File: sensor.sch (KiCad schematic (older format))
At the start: 6 parts

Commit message: switched to sensor sheet for one sensor divider
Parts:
- gave numbers to parts that had none: 6

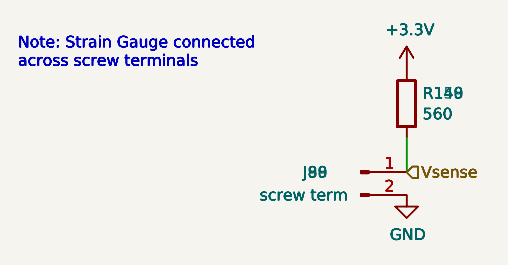
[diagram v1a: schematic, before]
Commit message: updated screw terminals to 2.54mm
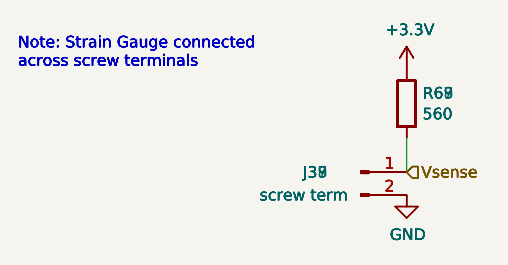
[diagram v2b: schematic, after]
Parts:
- J3: footprint Connector_PinHeader_1.27mm:PinHeader_1x02_P1.27mm_Vertical -> Connector_PinHeader_2.54mm:PinHeader_1x02_P2.54mm_Vertical
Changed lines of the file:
@@
 $Descr A4 11693 8268
 encoding utf-8
-Sheet 3 41
+Sheet 19 41
 Title ""
 Date ""
@@
 AR Path="/601B4C19/601A6FD1/6019C1B1" Ref="#PWR0181"  Part="1"
 AR Path="/601B4C19/601A6FD6/6019C1B1" Ref="#PWR0187"  Part="1"
-F 0 "#PWR0233" H 5400 3350 50  0001 C CNN
+F 0 "#PWR0110" H 5400 3350 50  0001 C CNN
 F 1 "GND" H 5405 3427 50  0000 C CNN
 F 2 "" H 5400 3600 50  0001 C CNN
@@
 AR Path="/601B4C19/601A6FD1/6019C1B2" Ref="R117"  Part="1"
 AR Path="/601B4C19/601A6FD6/6019C1B2" Ref="R120"  Part="1"
-F 0 "R150" H 5470 3246 50  0000 L CNN
+F 0 "R69" H 5470 3246 50  0000 L CNN
 F 1 "560" H 5470 3155 50  0000 L CNN
 F 2 "Resistor_THT:R_Axial_DIN0204_L3.6mm_D1.6mm_P5.08mm_Horizontal" V 5330 3200 50  0001 C CNN
@@
 AR Path="/601B4C19/601A6FD1/6019C1B3" Ref="J69"  Part="1"
 AR Path="/601B4C19/601A6FD6/6019C1B3" Ref="J72"  Part="1"
-F 0 "J90" H 5000 3500 50  0000 C CNN
+F 0 "J39" H 5000 3500 50  0000 C CNN
 F 1 "screw term" H 4950 3400 50  0000 C CNN
-F 2 "Connector_PinHeader_1.27mm:PinHeader_1x02_P1.27mm_Vertical" H 5200 3500 50  0001 C CNN
+F 2 "Connector_PinHeader_2.54mm:PinHeader_1x02_P2.54mm_Vertical" H 5200 3500 50  0001 C CNN
 F 3 "~" H 5200 3500 50  0001 C CNN
 	1    5200 3500
@@
 AR Path="/601B4C19/601A6FD1/601968DA" Ref="#PWR0176"  Part="1"
 AR Path="/601B4C19/601A6FD6/601968DA" Ref="#PWR0182"  Part="1"
-F 0 "#PWR0228" H 5400 2900 50  0001 C CNN
+F 0 "#PWR0105" H 5400 2900 50  0001 C CNN
 F 1 "+3.3V" H 5415 3223 50  0000 C CNN
 F 2 "" H 5400 3050 50  0001 C CNN
@@
 AR Path="/601B4C19/601A6FD1/6019BD32" Ref="#PWR0180"  Part="1"
 AR Path="/601B4C19/601A6FD6/6019BD32" Ref="#PWR0186"  Part="1"
-F 0 "#PWR0232" H 5400 3350 50  0001 C CNN
+F 0 "#PWR0109" H 5400 3350 50  0001 C CNN
 F 1 "GND" H 5405 3427 50  0000 C CNN
 F 2 "" H 5400 3600 50  0001 C CNN
@@
 AR Path="/601B4C19/601A6FD1/6019BD33" Ref="R116"  Part="1"
 AR Path="/601B4C19/601A6FD6/6019BD33" Ref="R119"  Part="1"
-F 0 "R149" H 5470 3246 50  0000 L CNN
+F 0 "R68" H 5470 3246 50  0000 L CNN
 F 1 "560" H 5470 3155 50  0000 L CNN
 F 2 "Resistor_THT:R_Axial_DIN0204_L3.6mm_D1.6mm_P5.08mm_Horizontal" V 5330 3200 50  0001 C CNN
@@
 AR Path="/601B4C19/601A6FD1/6019BD34" Ref="J68"  Part="1"
 AR Path="/601B4C19/601A6FD6/6019BD34" Ref="J71"  Part="1"
-F 0 "J89" H 5000 3500 50  0000 C CNN
+F 0 "J38" H 5000 3500 50  0000 C CNN
 F 1 "screw term" H 4950 3400 50  0000 C CNN
 F 2 "Connector_PinHeader_1.27mm:PinHeader_1x02_P1.27mm_Vertical" H 5200 3500 50  0001 C CNN
@@
 	1    0    0    -1
 $EndComp
-Wire Wire Line
-	5400 3350 5400 3500
 $Comp
 L power:+3.3V #PWR016
@@
 AR Path="/601B4C19/601A6FD1/6019BD35" Ref="#PWR0177"  Part="1"
 AR Path="/601B4C19/601A6FD6/6019BD35" Ref="#PWR0183"  Part="1"
-F 0 "#PWR0229" H 5400 2900 50  0001 C CNN
+F 0 "#PWR0106" H 5400 2900 50  0001 C CNN
 F 1 "+3.3V" H 5415 3223 50  0000 C CNN
 F 2 "" H 5400 3050 50  0001 C CNN
@@
 AR Path="/601B4C19/601A6FD1/60194B46" Ref="#PWR0179"  Part="1"
 AR Path="/601B4C19/601A6FD6/60194B46" Ref="#PWR0185"  Part="1"
-F 0 "#PWR0231" H 5400 3350 50  0001 C CNN
+F 0 "#PWR0108" H 5400 3350 50  0001 C CNN
 F 1 "GND" H 5405 3427 50  0000 C CNN
 F 2 "" H 5400 3600 50  0001 C CNN
@@
 AR Path="/601B4C19/601A6FD1/60194B4C" Ref="R115"  Part="1"
 AR Path="/601B4C19/601A6FD6/60194B4C" Ref="R118"  Part="1"
-F 0 "R148" H 5470 3246 50  0000 L CNN
+F 0 "R67" H 5470 3246 50  0000 L CNN
 F 1 "560" H 5470 3155 50  0000 L CNN
 F 2 "Resistor_THT:R_Axial_DIN0204_L3.6mm_D1.6mm_P5.08mm_Horizontal" V 5330 3200 50  0001 C CNN
@@
 AR Path="/601B4C19/601A6FD1/60194E45" Ref="J67"  Part="1"
 AR Path="/601B4C19/601A6FD6/60194E45" Ref="J70"  Part="1"
-F 0 "J88" H 5000 3500 50  0000 C CNN
+F 0 "J37" H 5000 3500 50  0000 C CNN
 F 1 "screw term" H 4950 3400 50  0000 C CNN
 F 2 "Connector_PinHeader_1.27mm:PinHeader_1x02_P1.27mm_Vertical" H 5200 3500 50  0001 C CNN
@@
 	1    0    0    -1
 $EndComp
-Wire Wire Line
-	5400 3350 5400 3500
 $Comp
 L power:+3.3V #PWR017
@@
 AR Path="/601B4C19/601A6FD1/6019C1B4" Ref="#PWR0178"  Part="1"
 AR Path="/601B4C19/601A6FD6/6019C1B4" Ref="#PWR0184"  Part="1"
-F 0 "#PWR0230" H 5400 2900 50  0001 C CNN
+F 0 "#PWR0107" H 5400 2900 50  0001 C CNN
 F 1 "+3.3V" H 5415 3223 50  0000 C CNN
 F 2 "" H 5400 3050 50  0001 C CNN

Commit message: removed stacked components
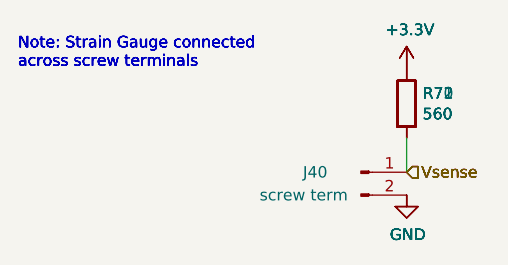
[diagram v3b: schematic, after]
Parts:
- removed J2: screw term, Connector_PinHeader_1.27mm:PinHeader_1x02_P1.27mm_Vertical, symbol Connector:Conn_01x02_Male
- removed J3: screw term, Connector_PinHeader_2.54mm:PinHeader_1x02_P2.54mm_Vertical, symbol Connector:Conn_01x02_Male
- J1: footprint Connector_PinHeader_1.27mm:PinHeader_1x02_P1.27mm_Vertical -> Connector_PinHeader_2.54mm:PinHeader_1x02_P2.54mm_Vertical
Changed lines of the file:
@@
 $Descr A4 11693 8268
 encoding utf-8
-Sheet 19 41
+Sheet 3 41
 Title ""
 Date ""
@@
 AR Path="/601B4C19/601A6FD1/6019C1B1" Ref="#PWR0181"  Part="1"
 AR Path="/601B4C19/601A6FD6/6019C1B1" Ref="#PWR0187"  Part="1"
-F 0 "#PWR0110" H 5400 3350 50  0001 C CNN
+F 0 "#PWR0116" H 5400 3350 50  0001 C CNN
 F 1 "GND" H 5405 3427 50  0000 C CNN
 F 2 "" H 5400 3600 50  0001 C CNN
@@
 AR Path="/601B4C19/601A6FD1/6019C1B2" Ref="R117"  Part="1"
 AR Path="/601B4C19/601A6FD6/6019C1B2" Ref="R120"  Part="1"
-F 0 "R69" H 5470 3246 50  0000 L CNN
+F 0 "R72" H 5470 3246 50  0000 L CNN
 F 1 "560" H 5470 3155 50  0000 L CNN
 F 2 "Resistor_THT:R_Axial_DIN0204_L3.6mm_D1.6mm_P5.08mm_Horizontal" V 5330 3200 50  0001 C CNN
 F 3 "~" H 5400 3200 50  0001 C CNN
 	1    5400 3200
-	1    0    0    -1
-$EndComp
-$Comp
-L Connector:Conn_01x02_Male J3
-U 1 1 6019C1B3
-P 5200 3500
-AR Path="/6017CC5E/60194350/6019C1B3" Ref="J3"  Part="1"
-AR Path="/6017CC5E/6019B999/6019C1B3" Ref="J6"  Part="1"
-AR Path="/601B4C0E/60194350/6019C1B3" Ref="J39"  Part="1"
-AR Path="/601B4C0E/6019B999/6019C1B3" Ref="J42"  Part="1"
-AR Path="/601B73B7/60194350/6019C1B3" Ref="J75"  Part="1"
-AR Path="/601B73B7/6019B999/6019C1B3" Ref="J78"  Part="1"
-AR Path="/6017CC5E/6019BDB6/6019C1B3" Ref="J9"  Part="1"
-AR Path="/601B4C0E/6019BDB6/6019C1B3" Ref="J45"  Part="1"
-AR Path="/601B73B7/6019BDB6/6019C1B3" Ref="J81"  Part="1"
-AR Path="/601927EB/601A1EA6/6019C1B3" Ref="J12"  Part="1"
-AR Path="/601927EB/601A1EAB/6019C1B3" Ref="J15"  Part="1"
-AR Path="/601927EB/601A1EB0/6019C1B3" Ref="J18"  Part="1"
-AR Path="/601B4C11/601A1EA6/6019C1B3" Ref="J48"  Part="1"
-AR Path="/601B4C11/601A1EAB/6019C1B3" Ref="J51"  Part="1"
-AR Path="/601B4C11/601A1EB0/6019C1B3" Ref="J54"  Part="1"
-AR Path="/601B73BA/601A1EA6/6019C1B3" Ref="J84"  Part="1"
-AR Path="/601B73BA/601A1EAB/6019C1B3" Ref="J87"  Part="1"
-AR Path="/601B73BA/601A1EB0/6019C1B3" Ref="J90"  Part="1"
-AR Path="/6019C043/601A47AA/6019C1B3" Ref="J21"  Part="1"
-AR Path="/6019C043/601A47AF/6019C1B3" Ref="J24"  Part="1"
-AR Path="/6019C043/601A47B4/6019C1B3" Ref="J27"  Part="1"
-AR Path="/601B4C16/601A47AA/6019C1B3" Ref="J57"  Part="1"
-AR Path="/601B4C16/601A47AF/6019C1B3" Ref="J60"  Part="1"
-AR Path="/601B4C16/601A47B4/6019C1B3" Ref="J63"  Part="1"
-AR Path="/6019DBCE/601A6FCC/6019C1B3" Ref="J30"  Part="1"
-AR Path="/6019DBCE/601A6FD1/6019C1B3" Ref="J33"  Part="1"
-AR Path="/6019DBCE/601A6FD6/6019C1B3" Ref="J36"  Part="1"
-AR Path="/601B4C19/601A6FCC/6019C1B3" Ref="J66"  Part="1"
-AR Path="/601B4C19/601A6FD1/6019C1B3" Ref="J69"  Part="1"
-AR Path="/601B4C19/601A6FD6/6019C1B3" Ref="J72"  Part="1"
-F 0 "J39" H 5000 3500 50  0000 C CNN
-F 1 "screw term" H 4950 3400 50  0000 C CNN
-F 2 "Connector_PinHeader_2.54mm:PinHeader_1x02_P2.54mm_Vertical" H 5200 3500 50  0001 C CNN
-F 3 "~" H 5200 3500 50  0001 C CNN
-	1    5200 3500
 	1    0    0    -1
 $EndComp
@@
 AR Path="/601B4C19/601A6FD1/601968DA" Ref="#PWR0176"  Part="1"
 AR Path="/601B4C19/601A6FD6/601968DA" Ref="#PWR0182"  Part="1"
-F 0 "#PWR0105" H 5400 2900 50  0001 C CNN
+F 0 "#PWR0111" H 5400 2900 50  0001 C CNN
 F 1 "+3.3V" H 5415 3223 50  0000 C CNN
 F 2 "" H 5400 3050 50  0001 C CNN
@@
 AR Path="/601B4C19/601A6FD1/6019BD32" Ref="#PWR0180"  Part="1"
 AR Path="/601B4C19/601A6FD6/6019BD32" Ref="#PWR0186"  Part="1"
-F 0 "#PWR0109" H 5400 3350 50  0001 C CNN
+F 0 "#PWR0115" H 5400 3350 50  0001 C CNN
 F 1 "GND" H 5405 3427 50  0000 C CNN
 F 2 "" H 5400 3600 50  0001 C CNN
@@
 AR Path="/601B4C19/601A6FD1/6019BD33" Ref="R116"  Part="1"
 AR Path="/601B4C19/601A6FD6/6019BD33" Ref="R119"  Part="1"
-F 0 "R68" H 5470 3246 50  0000 L CNN
+F 0 "R71" H 5470 3246 50  0000 L CNN
 F 1 "560" H 5470 3155 50  0000 L CNN
 F 2 "Resistor_THT:R_Axial_DIN0204_L3.6mm_D1.6mm_P5.08mm_Horizontal" V 5330 3200 50  0001 C CNN
 F 3 "~" H 5400 3200 50  0001 C CNN
 	1    5400 3200
-	1    0    0    -1
-$EndComp
-$Comp
-L Connector:Conn_01x02_Male J2
-U 1 1 6019BD34
-P 5200 3500
-AR Path="/6017CC5E/60194350/6019BD34" Ref="J2"  Part="1"
-AR Path="/6017CC5E/6019B999/6019BD34" Ref="J5"  Part="1"
-AR Path="/6017CC5E/6019BDB6/6019BD34" Ref="J8"  Part="1"
-AR Path="/601B4C0E/60194350/6019BD34" Ref="J38"  Part="1"
-AR Path="/601B4C0E/6019B999/6019BD34" Ref="J41"  Part="1"
-AR Path="/601B4C0E/6019BDB6/6019BD34" Ref="J44"  Part="1"
-AR Path="/601B73B7/60194350/6019BD34" Ref="J74"  Part="1"
-AR Path="/601B73B7/6019B999/6019BD34" Ref="J77"  Part="1"
-AR Path="/601B73B7/6019BDB6/6019BD34" Ref="J80"  Part="1"
-AR Path="/601927EB/601A1EA6/6019BD34" Ref="J11"  Part="1"
-AR Path="/601927EB/601A1EAB/6019BD34" Ref="J14"  Part="1"
-AR Path="/601927EB/601A1EB0/6019BD34" Ref="J17"  Part="1"
-AR Path="/601B4C11/601A1EA6/6019BD34" Ref="J47"  Part="1"
-AR Path="/601B4C11/601A1EAB/6019BD34" Ref="J50"  Part="1"
-AR Path="/601B4C11/601A1EB0/6019BD34" Ref="J53"  Part="1"
-AR Path="/601B73BA/601A1EA6/6019BD34" Ref="J83"  Part="1"
-AR Path="/601B73BA/601A1EAB/6019BD34" Ref="J86"  Part="1"
-AR Path="/601B73BA/601A1EB0/6019BD34" Ref="J89"  Part="1"
-AR Path="/6019C043/601A47AA/6019BD34" Ref="J20"  Part="1"
-AR Path="/6019C043/601A47AF/6019BD34" Ref="J23"  Part="1"
-AR Path="/6019C043/601A47B4/6019BD34" Ref="J26"  Part="1"
-AR Path="/601B4C16/601A47AA/6019BD34" Ref="J56"  Part="1"
-AR Path="/601B4C16/601A47AF/6019BD34" Ref="J59"  Part="1"
-AR Path="/601B4C16/601A47B4/6019BD34" Ref="J62"  Part="1"
-AR Path="/6019DBCE/601A6FCC/6019BD34" Ref="J29"  Part="1"
-AR Path="/6019DBCE/601A6FD1/6019BD34" Ref="J32"  Part="1"
-AR Path="/6019DBCE/601A6FD6/6019BD34" Ref="J35"  Part="1"
-AR Path="/601B4C19/601A6FCC/6019BD34" Ref="J65"  Part="1"
-AR Path="/601B4C19/601A6FD1/6019BD34" Ref="J68"  Part="1"
-AR Path="/601B4C19/601A6FD6/6019BD34" Ref="J71"  Part="1"
-F 0 "J38" H 5000 3500 50  0000 C CNN
-F 1 "screw term" H 4950 3400 50  0000 C CNN
-F 2 "Connector_PinHeader_1.27mm:PinHeader_1x02_P1.27mm_Vertical" H 5200 3500 50  0001 C CNN
-F 3 "~" H 5200 3500 50  0001 C CNN
-	1    5200 3500
 	1    0    0    -1
 $EndComp
@@
 AR Path="/601B4C19/601A6FD1/6019BD35" Ref="#PWR0177"  Part="1"
 AR Path="/601B4C19/601A6FD6/6019BD35" Ref="#PWR0183"  Part="1"
-F 0 "#PWR0106" H 5400 2900 50  0001 C CNN
+F 0 "#PWR0112" H 5400 2900 50  0001 C CNN
 F 1 "+3.3V" H 5415 3223 50  0000 C CNN
 F 2 "" H 5400 3050 50  0001 C CNN
@@
 AR Path="/601B4C19/601A6FD1/60194B46" Ref="#PWR0179"  Part="1"
 AR Path="/601B4C19/601A6FD6/60194B46" Ref="#PWR0185"  Part="1"
-F 0 "#PWR0108" H 5400 3350 50  0001 C CNN
+F 0 "#PWR0114" H 5400 3350 50  0001 C CNN
 F 1 "GND" H 5405 3427 50  0000 C CNN
 F 2 "" H 5400 3600 50  0001 C CNN
@@
 AR Path="/601B4C19/601A6FD1/60194B4C" Ref="R115"  Part="1"
 AR Path="/601B4C19/601A6FD6/60194B4C" Ref="R118"  Part="1"
-F 0 "R67" H 5470 3246 50  0000 L CNN
+F 0 "R70" H 5470 3246 50  0000 L CNN
 F 1 "560" H 5470 3155 50  0000 L CNN
 F 2 "Resistor_THT:R_Axial_DIN0204_L3.6mm_D1.6mm_P5.08mm_Horizontal" V 5330 3200 50  0001 C CNN
@@
 AR Path="/601B4C19/601A6FD1/60194E45" Ref="J67"  Part="1"
 AR Path="/601B4C19/601A6FD6/60194E45" Ref="J70"  Part="1"
-F 0 "J37" H 5000 3500 50  0000 C CNN
+F 0 "J40" H 5000 3500 50  0000 C CNN
 F 1 "screw term" H 4950 3400 50  0000 C CNN
-F 2 "Connector_PinHeader_1.27mm:PinHeader_1x02_P1.27mm_Vertical" H 5200 3500 50  0001 C CNN
+F 2 "Connector_PinHeader_2.54mm:PinHeader_1x02_P2.54mm_Vertical" H 5200 3500 50  0001 C CNN
 F 3 "~" H 5200 3500 50  0001 C CNN
 	1    5200 3500
@@
 AR Path="/601B4C19/601A6FD1/6019C1B4" Ref="#PWR0178"  Part="1"
 AR Path="/601B4C19/601A6FD6/6019C1B4" Ref="#PWR0184"  Part="1"
-F 0 "#PWR0107" H 5400 2900 50  0001 C CNN
+F 0 "#PWR0113" H 5400 2900 50  0001 C CNN
 F 1 "+3.3V" H 5415 3223 50  0000 C CNN
 F 2 "" H 5400 3050 50  0001 C CNN

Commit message: revised sensor connector
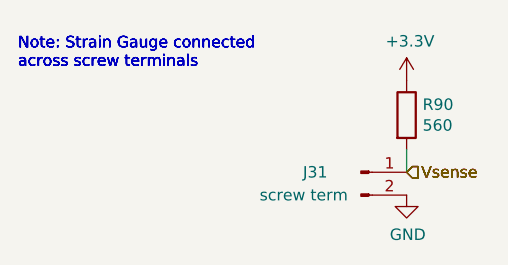
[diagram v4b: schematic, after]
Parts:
- removed R7, R8, R9: 560, Resistor_THT:R_Axial_DIN0204_L3.6mm_D1.6mm_P5.08mm_Horizontal, symbol Device:R
- added R44: 560, Resistor_THT:R_Axial_DIN0204_L3.6mm_D1.6mm_P5.08mm_Horizontal, symbol Device:R
- renumbered J1 to J2
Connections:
- net +3V3: now also R44.1
- net Vsense: now also R44.2

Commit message: removed sync signals
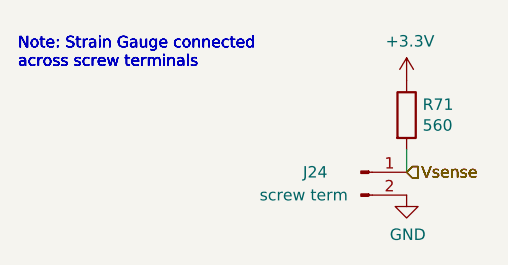
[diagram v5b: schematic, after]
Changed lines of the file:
@@
 $Descr A4 11693 8268
 encoding utf-8
-Sheet 3 41
+Sheet 32 41
 Title ""
 Date ""
@@
 AR Path="/601B4C19/601A6FD1/60194E45" Ref="J24"  Part="1"
 AR Path="/601B4C19/601A6FD6/60194E45" Ref="J25"  Part="1"
-F 0 "J31" H 5000 3500 50  0000 C CNN
+F 0 "J24" H 5000 3500 50  0000 C CNN
 F 1 "screw term" H 4950 3400 50  0000 C CNN
 F 2 "Connector_PinHeader_2.54mm:PinHeader_1x02_P2.54mm_Vertical" H 5200 3500 50  0001 C CNN
@@
 AR Path="/601B4C19/601A6FD1/60194B46" Ref="#PWR089"  Part="1"
 AR Path="/601B4C19/601A6FD6/60194B46" Ref="#PWR091"  Part="1"
-F 0 "#PWR0113" H 5400 3350 50  0001 C CNN
+F 0 "#PWR089" H 5400 3350 50  0001 C CNN
 F 1 "GND" H 5405 3427 50  0000 C CNN
 F 2 "" H 5400 3600 50  0001 C CNN
@@
 AR Path="/601B73BA/601A1EAB/601BA7A4" Ref="R89"  Part="1"
 AR Path="/601B73BA/601A1EB0/601BA7A4" Ref="R90"  Part="1"
-F 0 "R90" H 5470 3296 50  0000 L CNN
+F 0 "R71" H 5470 3296 50  0000 L CNN
 F 1 "560" H 5470 3205 50  0000 L CNN
 F 2 "Resistor_THT:R_Axial_DIN0204_L3.6mm_D1.6mm_P5.08mm_Horizontal" V 5330 3250 50  0001 C CNN
@@
 AR Path="/601B73BA/601A1EAB/601BAE3C" Ref="#PWR0110"  Part="1"
 AR Path="/601B73BA/601A1EB0/601BAE3C" Ref="#PWR0112"  Part="1"
-F 0 "#PWR0112" H 5400 2950 50  0001 C CNN
+F 0 "#PWR088" H 5400 2950 50  0001 C CNN
 F 1 "+3.3V" H 5415 3273 50  0000 C CNN
 F 2 "" H 5400 3100 50  0001 C CNN

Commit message: moved sensor r div to other side of mux
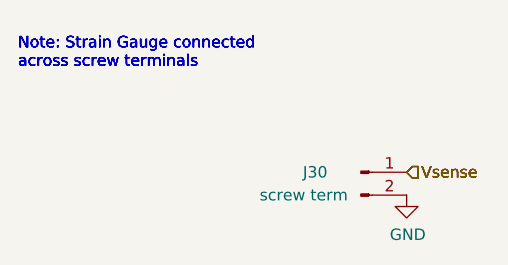
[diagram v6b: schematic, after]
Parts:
- removed R44: 560, Resistor_THT:R_Axial_DIN0204_L3.6mm_D1.6mm_P5.08mm_Horizontal, symbol Device:R
- renumbered J2 to J1

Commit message: updated strain gauge connection to solder pads
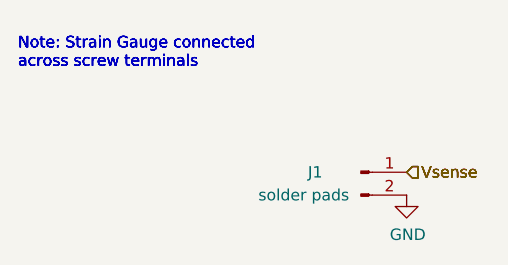
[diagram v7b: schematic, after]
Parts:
- J1: value screw term -> solder pads; footprint Connector_PinHeader_2.54mm:PinHeader_1x02_P2.54mm_Vertical -> TestPoint:TestPoint_Pad_2.0x2.0mm
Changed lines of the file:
@@
 AR Path="/601B4C19/601A6FD1/60194E45" Ref="J23"  Part="1"
 AR Path="/601B4C19/601A6FD6/60194E45" Ref="J24"  Part="1"
-F 0 "J30" H 5000 3500 50  0000 C CNN
-F 1 "screw term" H 4950 3400 50  0000 C CNN
-F 2 "Connector_PinHeader_2.54mm:PinHeader_1x02_P2.54mm_Vertical" H 5200 3500 50  0001 C CNN
+F 0 "J1" H 5000 3500 50  0000 C CNN
+F 1 "solder pads" H 4950 3400 50  0000 C CNN
+F 2 "TestPoint:TestPoint_Pad_2.0x2.0mm" H 5200 3500 50  0001 C CNN
 F 3 "~" H 5200 3500 50  0001 C CNN
 	1    5200 3500
@@
 AR Path="/601B4C19/601A6FD1/60194B46" Ref="#PWR074"  Part="1"
 AR Path="/601B4C19/601A6FD6/60194B46" Ref="#PWR075"  Part="1"
-F 0 "#PWR093" H 5400 3350 50  0001 C CNN
+F 0 "#PWR016" H 5400 3350 50  0001 C CNN
 F 1 "GND" H 5405 3427 50  0000 C CNN
 F 2 "" H 5400 3600 50  0001 C CNN
